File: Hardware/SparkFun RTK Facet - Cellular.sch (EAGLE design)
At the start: 64 parts, among them IC1 SN74AVC4T774PW, J1 FPC_12_0.5MM_BACKFLIP, J18 SARA_USB, J2 NANO_SIM, J3 U.FL, J6 DIAG, Q2 310mA/60V/1.6Ω, Q3 310mA/60V/1.6Ω, Q4 310mA/60V/1.6Ω, Q5 20V/0.2A/8MHz/1.2Ω/1Vth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

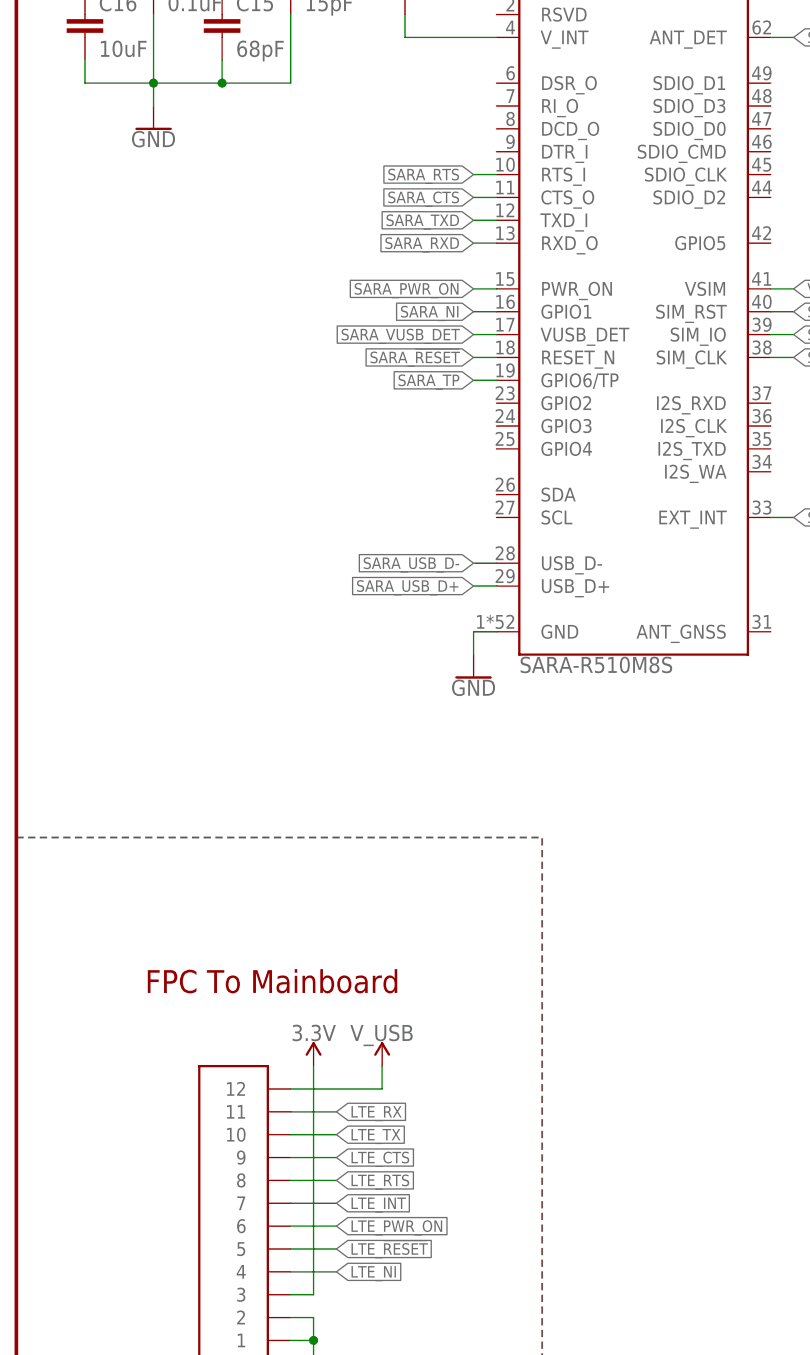
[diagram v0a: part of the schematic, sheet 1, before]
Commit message: Net rename to indicate inputs vs outputs
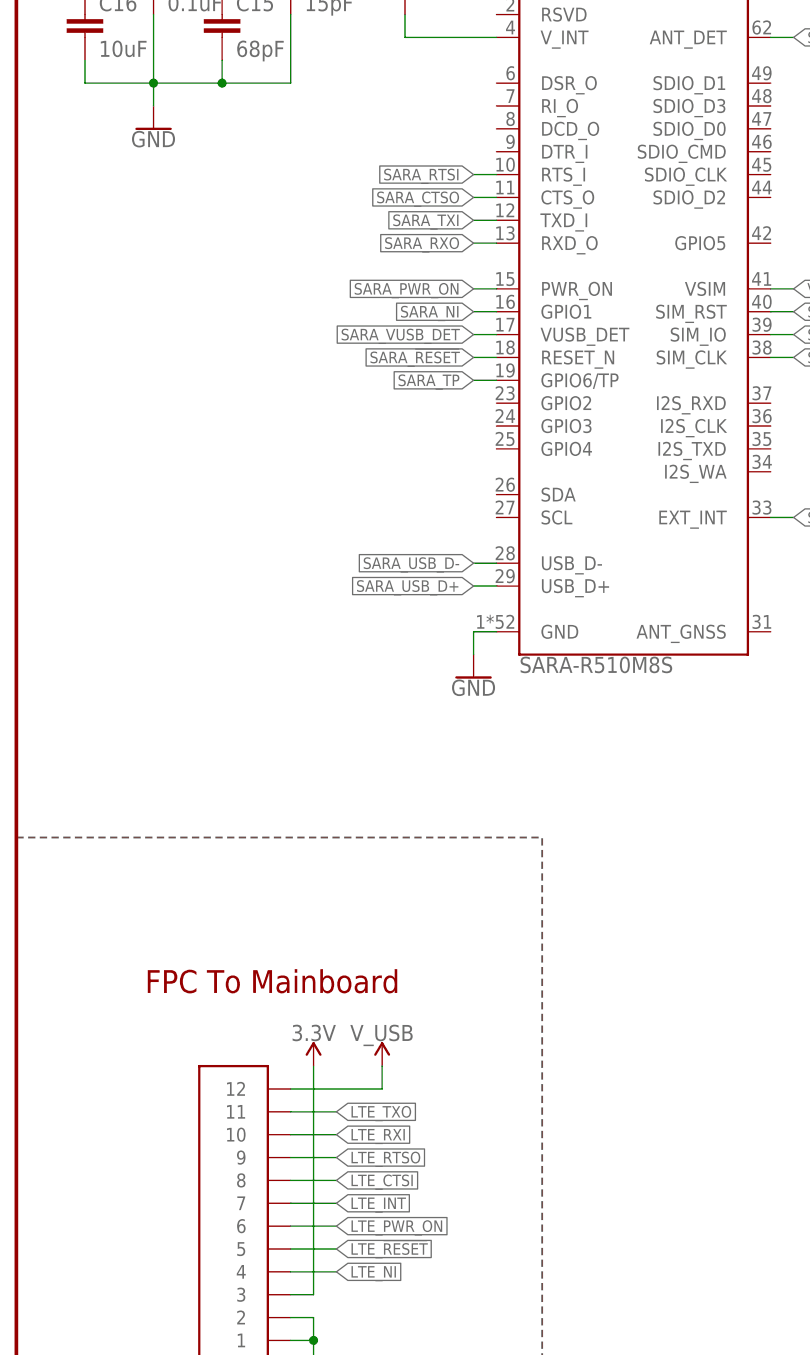
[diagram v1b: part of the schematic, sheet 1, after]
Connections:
- net LTE_CTS renamed LTE_RTSO
- net LTE_RTS renamed LTE_CTSI
- net LTE_RX renamed LTE_TXO
- net LTE_TX renamed LTE_RXI
- net SARA_CTS renamed SARA_CTSO
- net SARA_RTS renamed SARA_RTSI
- net SARA_RXD renamed SARA_RXO
- net SARA_TXD renamed SARA_TXI
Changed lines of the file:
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@@
 </segment>
 </net>
-<net name="LTE_RTS" class="0">
+<net name="LTE_CTSI" class="0">
 <segment>
 <wire x1="30.48" y1="33.02" x2="35.56" y2="33.02" width="0.1524" layer="91"/>
@@
 </segment>
 </net>
-<net name="LTE_RX" class="0">
+<net name="LTE_TXO" class="0">
 <segment>
 <wire x1="30.48" y1="40.64" x2="35.56" y2="40.64" width="0.1524" layer="91"/>
@@
 </segment>
 </net>
-<net name="LTE_CTS" class="0">
+<net name="LTE_RTSO" class="0">
 <segment>
 <wire x1="30.48" y1="35.56" x2="35.56" y2="35.56" width="0.1524" layer="91"/>
@@
 </segment>
 </net>
-<net name="LTE_TX" class="0">
+<net name="LTE_RXI" class="0">
 <segment>
 <wire x1="30.48" y1="38.1" x2="35.56" y2="38.1" width="0.1524" layer="91"/>
@@
 </segment>
 </net>
-<net name="SARA_RTS" class="0">
+<net name="SARA_RTSI" class="0">
 <segment>
 <pinref part="U1" gate="G$2" pin="RTS_I"/>
@@
 </segment>
 </net>
-<net name="SARA_CTS" class="0">
+<net name="SARA_CTSO" class="0">
 <segment>
 <pinref part="U1" gate="G$2" pin="CTS_O"/>
@@
 </segment>
 </net>
-<net name="SARA_TXD" class="0">
+<net name="SARA_TXI" class="0">
 <segment>
 <label x="50.8" y="139.7" size="1.27" layer="95" rot="R180" xref="yes"/>
@@
 </segment>
 </net>
-<net name="SARA_RXD" class="0">
+<net name="SARA_RXO" class="0">
 <segment>
 <label x="50.8" y="137.16" size="1.27" layer="95" rot="R180" xref="yes"/>
@@
 </segment>
 </net>
-<net name="LTE_TX" class="0">
+<net name="LTE_RXI" class="0">
 <segment>
 <label x="373.38" y="142.24" size="1.27" layer="95" xref="yes"/>
@@
 </segment>
 </net>
-<net name="LTE_CTS" class="0">
+<net name="LTE_RTSO" class="0">
 <segment>
 <label x="373.38" y="139.7" size="1.27" layer="95" xref="yes"/>
@@
 </segment>
 </net>
-<net name="LTE_RTS" class="0">
+<net name="LTE_CTSI" class="0">
 <segment>
 <label x="373.38" y="137.16" size="1.27" layer="95" xref="yes"/>
@@
 </segment>
 </net>
-<net name="SARA_RXD" class="0">
+<net name="SARA_RXO" class="0">
 <segment>
 <label x="289.56" y="144.78" size="1.27" layer="95" rot="R180" xref="yes"/>
@@
 </segment>
 </net>
-<net name="SARA_TXD" class="0">
+<net name="SARA_TXI" class="0">
 <segment>
 <label x="289.56" y="142.24" size="1.27" layer="95" rot="R180" xref="yes"/>
@@
 </segment>
 </net>
-<net name="SARA_CTS" class="0">
+<net name="SARA_CTSO" class="0">
 <segment>
 <label x="289.56" y="139.7" size="1.27" layer="95" rot="R180" xref="yes"/>
@@
 </segment>
 </net>
-<net name="SARA_RTS" class="0">
+<net name="SARA_RTSI" class="0">
 <segment>
 <label x="289.56" y="137.16" size="1.27" layer="95" rot="R180" xref="yes"/>
@@
 </segment>
 </net>
-<net name="LTE_RX" class="0">
+<net name="LTE_TXO" class="0">
 <segment>
 <label x="373.38" y="144.78" size="1.27" layer="95" xref="yes"/>
